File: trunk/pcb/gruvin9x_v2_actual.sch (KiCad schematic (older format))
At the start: 140 parts, among them P2 CONN_5, P3 CONN_6, P4 CONN_9, P5 CONN_9, P6 CONN_6, P7 CONN_12, P8 CONN_30, Q1 2SC9014, SW1 SW_PUSH, SW2 SW_PUSH, SW3 SW_PUSH, SW4 SW_PUSH, SW5 SW_PUSH, SW6 SW_PUSH, U1 78L05, U2 4066, U3 LN-6206-30, X1 16MHz

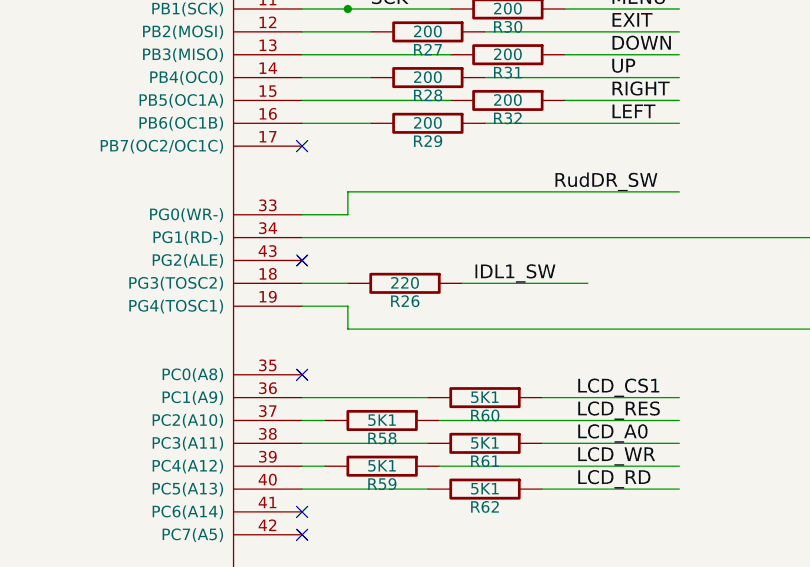
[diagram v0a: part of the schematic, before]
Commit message: PCB files update - now includes custom components source files
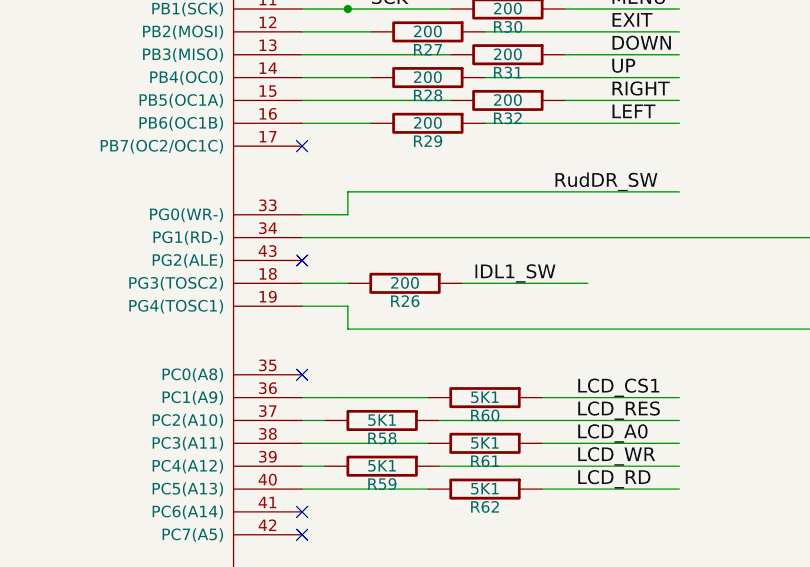
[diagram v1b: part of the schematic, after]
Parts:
- R26: value 220 -> 200
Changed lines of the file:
@@
-EESchema Schematic File Version 2  date 25/11/2010 10:01:41 a.m.
+EESchema Schematic File Version 2  date 26/11/2010 9:53:01 a.m.
 LIBS:power
 LIBS:device
@@
 Sheet 1 1
 Title "Main Controller PCB (Stock)"
-Date "24 nov 2010"
-Rev "1.0"
+Date "25 nov 2010"
+Rev "1.1"
 Comp "gruvin9x"
 Comment1 "(Layout designed to suit easy conversion to 2xA4 if required.)"
@@
 P 6500 8600
 F 0 "R26" V 6580 8600 50  0000 C CNN
-F 1 "220" V 6500 8600 50  0000 C CNN
+F 1 "200" V 6500 8600 50  0000 C CNN
 	1    6500 8600
 	0    1    1    0

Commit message: PCB rev2.1 final_draft (gruvin9x.brd/sch) uploaded
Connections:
- net labels added: TCut_SW
- net labels removed: ADROT
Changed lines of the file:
@@
-EESchema Schematic File Version 2  date 26/11/2010 9:53:01 a.m.
+EESchema Schematic File Version 2  date 1/12/2010 4:57:59 p.m.
 LIBS:power
 LIBS:device
@@
 Sheet 1 1
 Title "Main Controller PCB (Stock)"
-Date "25 nov 2010"
+Date "1 dec 2010"
 Rev "1.1"
 Comp "gruvin9x"
@@
 $EndComp
 Text Label 13600 9850 0    60   ~ 0
-ADROT
+TCut_SW
 Text Label 13600 9750 0    60   ~ 0
 Hov_Pit
@@
 AilDR_SW
 Text Label 3250 2400 0    60   ~ 0
-ADROT
+TCut_SW
 $Comp
 L GND #PWR6
@@
 AilDR_SW
 Text Label 700  8200 0    60   ~ 0
-ADROT
+TCut_SW
 Text Label 700  8500 0    60   ~ 0
 Speaker
